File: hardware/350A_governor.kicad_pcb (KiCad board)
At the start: 2 copper layers, 100 x 80 mm, 18 parts, among them J1 CANNON_CONN, J2 PANEL_J2, J3 PANEL_J3, U1 6N137, U2 ULN2003A

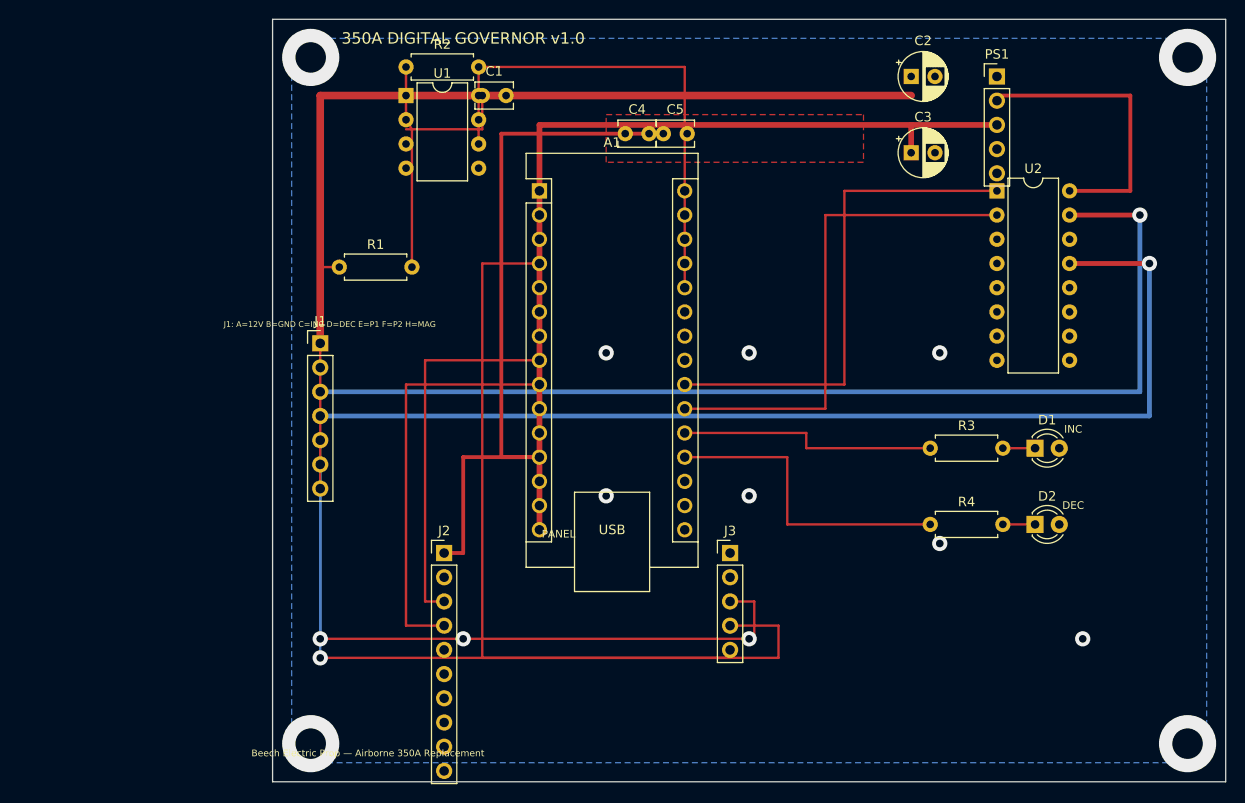
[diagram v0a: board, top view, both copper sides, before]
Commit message: Change in switch architecture
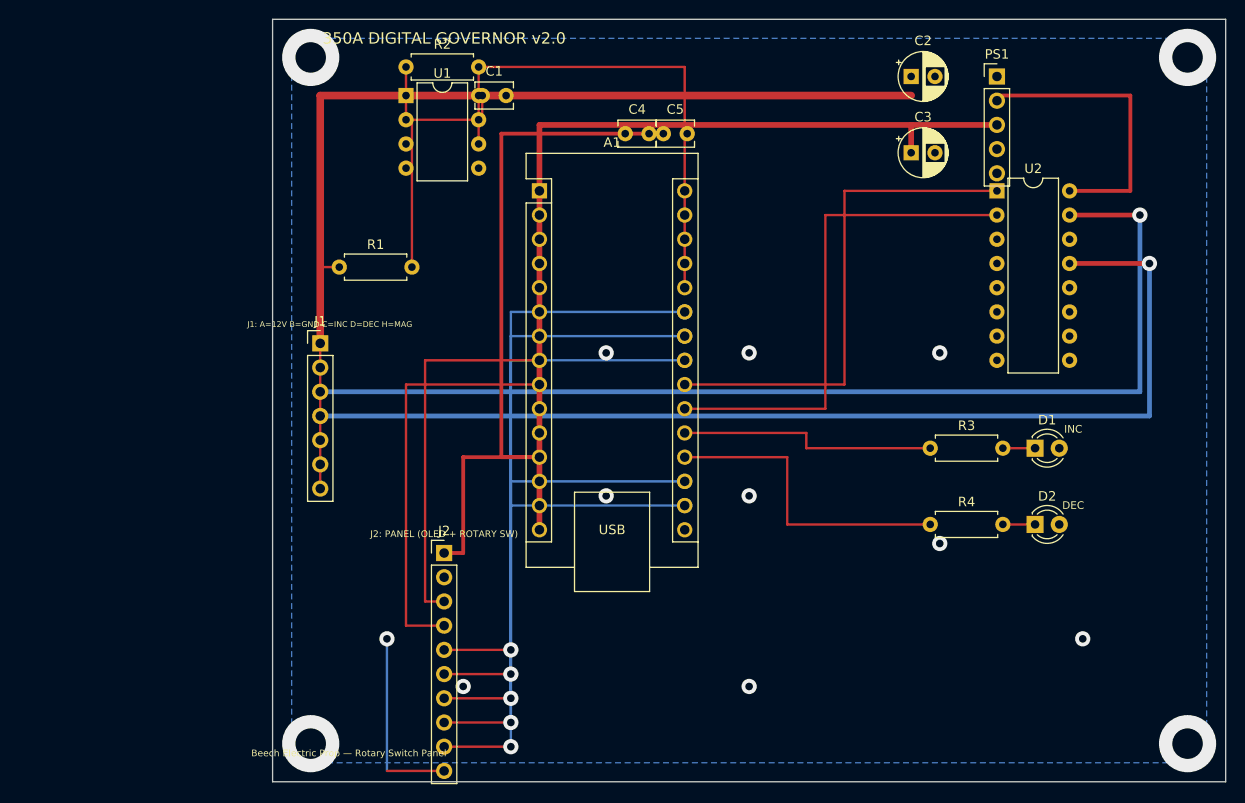
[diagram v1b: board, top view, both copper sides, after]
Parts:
- removed J3: PANEL_J3, PinHeader_1x05_P2.54mm_Vertical
- J1: value CANNON_CONN -> CANNON
- J2: value PANEL_J2 -> PANEL
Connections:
- net D10 renamed D10_SW4
- net D11 renamed D11_SW5
- A1 pad 16: D12 -> (no net)
- A1 pad 23: D5_ENC_B -> D5_SW3
- A1 pad 24: D4_ENC_A -> D4_SW2
- A1 pad 25: D3_ENC_SW -> D3_SW1
- A1 pad 4: A0_POT -> A0_NC
- A1 pad 5: A1 -> (no net)
- J1 pad 5: POT_E -> SW_COMMON
- J1 pad 6: POT_F -> NC
- J2 pad 10: D12 -> SW_COMMON
- J2 pad 5: D4_ENC_A -> D3_SW1
- J2 pad 6: D5_ENC_B -> D4_SW2
- J2 pad 7: D3_ENC_SW -> D5_SW3
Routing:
- net POT_F: track 76.8 -> 0.00 mm, vias 1 -> 0
- net A0_POT: track 73.4 -> 0.00 mm
- net POT_E: track 72.8 -> 0.00 mm, vias 1 -> 0
- net D4_SW2: track 0.00 -> 60.7 mm, vias 0 -> 2
- net D5_SW3: track 0.00 -> 60.7 mm, vias 0 -> 2
- net D3_SW1: track 0.00 -> 60.7 mm, vias 0 -> 2
- net D10_SW4: track 0.00 -> 50.5 mm, vias 0 -> 2
- net D11_SW5: track 0.00 -> 50.5 mm, vias 0 -> 2
- net SW_COMMON: track 0.00 -> 19.9 mm, vias 0 -> 1
- net MAG_A: track 27.2 -> 26.0 mm
- removed copper zone on F.Cu, net 5V
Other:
- board text added: "350A DIGITAL GOVERNOR v2.0"
- board text added: "Beech Electric Prop — Rotary Switch Panel"
- board text added: "J1: A=12V B=GND C=INC D=DEC H=MAG"
- board text added: "J2: PANEL (OLED + ROTARY SW)"
- board text removed: "350A DIGITAL GOVERNOR v1.0"
- board text removed: "Beech Electric Prop — Airborne 350A Replacement"
- board text removed: "J1: A=12V B=GND C=INC D=DEC E=P1 F=P2 H=MAG"
- board text removed: "PANEL"

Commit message: Fiverr design.
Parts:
- A1: value Arduino Nano -> Arduino_Nano
- C2: value 100uF -> 100uF/16V
- C3: value 47uF -> 47uF/10V
- J1: value CANNON -> CANNON_7PIN
- J2: value PANEL -> PANEL_10PIN
- moved J2 74.7 mm to (92.0, 46.0)
- moved C2 59.2 mm to (12.0, 28.0)
- moved R1 32.4 mm to (10.0, 58.2)
- moved U2 28.1 mm to (78.0, 46.0)
- moved C5 19.4 mm to (22.0, 8.00)
- moved C4 18.0 mm to (52.0, 22.0)
- moved C1 17.2 mm to (12.0, 22.0)
- moved R3 13.8 mm to (58.0, 53.4)
- moved C3 13.6 mm to (80.0, 10.0)
- moved D1 13.1 mm to (70.0, 53.4), turned to 180 degrees
- moved A1 12.2 mm to (35.0, 28.0)
- moved PS1 12.2 mm to (88.0, 8.00)
- moved R4 11.4 mm to (58.0, 55.9)
- moved R2 11.2 mm to (24.0, 10.0)
- moved D2 10.4 mm to (70.0, 55.9), turned to 180 degrees
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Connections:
- net DEC_OUT renamed DEC_RELAY
- net INC_OUT renamed INC_RELAY
- net MAG_A renamed MAG_FILT
- A1 pad 10: (no net) -> D7_DEC
- A1 pad 11: (no net) -> D8_INC_LED
- A1 pad 12: 5V -> D9_DEC_LED
- A1 pad 13: (no net) -> D10_SW4
- A1 pad 14: GND -> D11_SW5
- A1 pad 15: VIN_5V -> (no net)
- A1 pad 17: D11_SW5 -> (no net)
- A1 pad 18: D10_SW4 -> (no net)
- A1 pad 19: D9_DEC_LED -> (no net)
- A1 pad 20: D8_INC_LED -> (no net)
- A1 pad 21: D7_DEC -> (no net)
- A1 pad 22: D6_INC -> (no net)
- A1 pad 23: D5_SW3 -> SDA
- A1 pad 24: D4_SW2 -> SCL
- A1 pad 25: D3_SW1 -> (no net)
- A1 pad 26: D2_RPM -> (no net)
- A1 pad 27: GND -> VCC5
- A1 pad 29: (no net) -> GND
- A1 pad 30: (no net) -> VCC5
- A1 pad 4: A0_NC -> GND
- A1 pad 5: (no net) -> D2_RPM
- A1 pad 6: (no net) -> D3_SW1
- A1 pad 7: (no net) -> D4_SW2
- A1 pad 8: SDA -> D5_SW3
- A1 pad 9: SCL -> D6_INC
- C3 pad 1: VIN_5V -> VCC5
- C4 pad 1: VIN_5V -> VCC5
- C5 pad 1: 5V -> VCC5
- J1 pad 5: SW_COMMON -> GND
- J1 pad 6: NC -> (no net)
- J2 pad 1: 5V -> VCC5
- J2 pad 10: SW_COMMON -> GND
- PS1 pad 3: VIN_5V -> VCC5
- R2 pad 1: 5V -> VCC5
- R2 pad 2: RPM_PULSE -> D2_RPM
- U1 pad 5: 5V -> VCC5
- U1 pad 6: RPM_PULSE -> D2_RPM
- U1 pad 8: 5V -> VCC5
- U2 pad 9: (no net) -> 12V_COM
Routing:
- net INC_RELAY: track 111.9 -> 0.00 mm, vias 2 -> 0
- net DEC_RELAY: track 111.4 -> 0.00 mm, vias 2 -> 0
- net VIN_5V: track 94.3 -> 0.00 mm
- net 12V_RAW: track 88.0 -> 0.00 mm
- net 5V: track 81.1 -> 0.00 mm
- net D4_SW2: track 60.7 -> 0.00 mm, vias 2 -> 0
- net D5_SW3: track 60.7 -> 0.00 mm, vias 2 -> 0
- net D3_SW1: track 60.7 -> 0.00 mm, vias 2 -> 0
- net D7_DEC: track 53.1 -> 0.00 mm
- net D6_INC: track 53.1 -> 0.00 mm
- net RPM_PULSE: track 52.9 -> 0.00 mm
- net D10_SW4: track 50.5 -> 0.00 mm, vias 2 -> 0
- net D11_SW5: track 50.5 -> 0.00 mm, vias 2 -> 0
- net SCL: track 43.3 -> 0.00 mm
- net SDA: track 39.3 -> 0.00 mm
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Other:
- board text added: "J1: 1=12V 2=GND 3=INC 4=DEC 5=GND 7=MAG"
- board text added: "J2: 1=5V 2=GND 3=SDA 4=SCL 5-9=SW1-5 10=GND"
- board text added: "PS1: 1=12V 2=GND 3=5V 4=GND"
- board text added: "ROUTE THIS BOARD IN KICAD: File>Board Setup>Constraints then press N for ratsnest"
- board text removed: "Beech Electric Prop — Rotary Switch Panel"
- board text removed: "DEC"
- board text removed: "INC"
- board text removed: "J1: A=12V B=GND C=INC D=DEC H=MAG"
- board text removed: "J2: PANEL (OLED + ROTARY SW)"
